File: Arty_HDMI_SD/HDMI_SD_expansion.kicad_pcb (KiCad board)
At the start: 4 copper layers, 109 x 40 mm, 54 parts, among them J2 1140084168, J4 2000-1-2-41-00-BK, J5 UE27AC54100, U1 TPS61232DRCT, U2 MAX3421EEHJ, Y1 KX-7_12,MHz

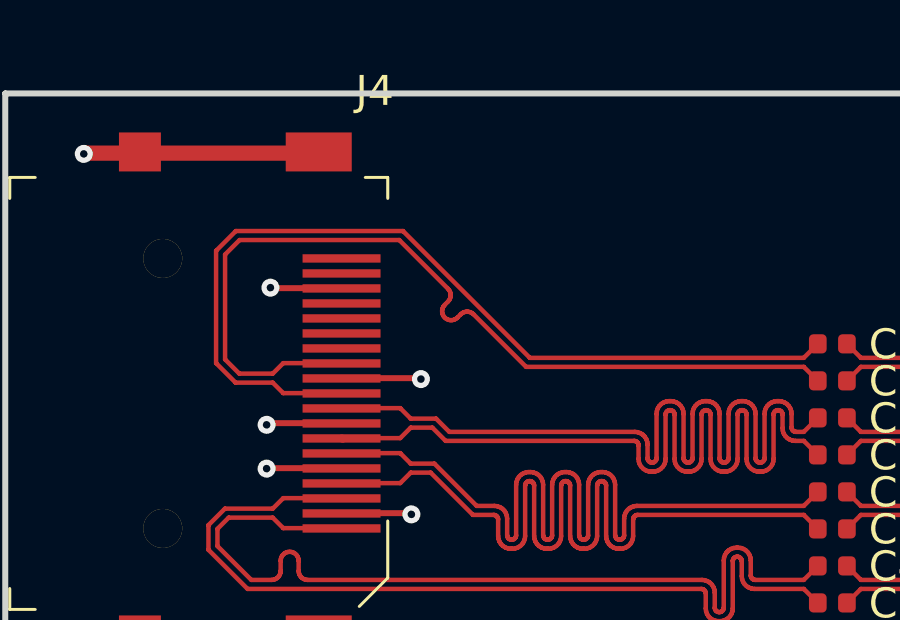
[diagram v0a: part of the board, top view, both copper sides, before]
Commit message: Added more testpads
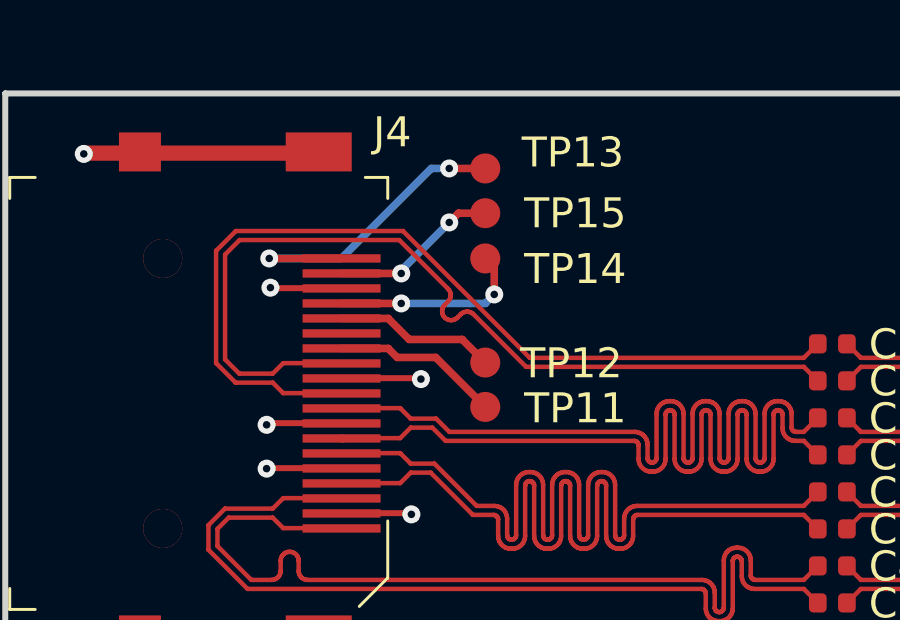
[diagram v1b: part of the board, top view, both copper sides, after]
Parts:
- added TP11: TP_SMD1MM, antmicro-footprints:Testpoint_smd_1mm, F.Cu at (107.7, 95.0)
- added TP12: TP_SMD1MM, antmicro-footprints:Testpoint_smd_1mm, F.Cu at (107.7, 93.5)
- added TP13: TP_SMD1MM, antmicro-footprints:Testpoint_smd_1mm, F.Cu at (107.7, 87.0)
- added TP14: TP_SMD1MM, antmicro-footprints:Testpoint_smd_1mm, F.Cu at (107.7, 90.0)
- added TP15: TP_SMD1MM, antmicro-footprints:Testpoint_smd_1mm, F.Cu at (107.7, 88.5)
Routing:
- net Net-(J4-Pad19): track 0.00 -> 10.9 mm, vias 0 -> 2
- net Net-(J4-Pad16): track 0.00 -> 6.54 mm, vias 0 -> 2
- net Net-(J4-Pad18): track 0.00 -> 5.68 mm, vias 0 -> 2
- net Net-(J4-Pad13): track 0.00 -> 5.60 mm
- net Net-(J4-Pad15): track 0.00 -> 5.40 mm
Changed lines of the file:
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@@
-(kicad_pcb (version 20171130) (host pcbnew 5.0.2+dfsg1-1)
+(kicad_pcb (version 20171130) (host pcbnew 5.0.2+dfsg1-1~bpo9+1)
   (general
     (thickness 1.6)
     (drawings 16)
-    (tracks 2859)
+    (tracks 2889)
     (zones 0)
-    (modules 54)
+    (modules 59)
     (nets 71)
   )
@@
     (1 In1.Cu signal hide)
     (2 In2.Cu signal hide)
-    (31 B.Cu signal hide)
+    (31 B.Cu signal)
     (32 B.Adhes user hide)
     (33 F.Adhes user hide)
@@
     (35 F.Paste user hide)
     (36 B.SilkS user hide)
-    (37 F.SilkS user hide)
+    (37 F.SilkS user)
     (38 B.Mask user hide)
     (39 F.Mask user hide)
@@
   )
   (setup
-    (last_trace_width 0.2)
+    (last_trace_width 0.254)
     (user_trace_width 0.2)
     (user_trace_width 0.508)
@@
     (add_net "Net-(U2-Pad9)")
   )
+  (module antmicro-footprints:Testpoint_smd_1mm (layer F.Cu)
+    (at 107.651241 94.978709)
+    (fp_text reference TP11 (at 3 0) (layer F.SilkS)
+      (effects (font (size 1 1) (thickness 0.15)))
+    )
+    (fp_text value TP_SMD1MM (at 0 -0.5) (layer F.Fab) hide
+      (effects (font (size 1 1) (thickness 0.15)))
+    )
+    (pad 1 smd circle (at 0 -0.0508) (size 1 1) (layers F.Cu F.Paste F.Mask)
+      (net 64 "Net-(J4-Pad13)"))
+  )
+  (module antmicro-footprints:Testpoint_smd_1mm (layer F.Cu)
+    (at 107.651241 93.499509)
+    (fp_text reference TP12 (at 2.87 -0.0208) (layer F.SilkS)
+      (effects (font (size 1 1) (thickness 0.15)))
+    )
+    (fp_text value TP_SMD1MM (at 0 -0.5) (layer F.Fab) hide
+      (effects (font (size 1 1) (thickness 0.15)))
+    )
+    (pad 1 smd circle (at 0 -0.0508) (size 1 1) (layers F.Cu F.Paste F.Mask)
+      (net 66 "Net-(J4-Pad15)"))
+  )
+  (module antmicro-footprints:Testpoint_smd_1mm (layer F.Cu)
+    (at 107.651241 90.029509)
+    (fp_text reference TP14 (at 3 0.3048) (layer F.SilkS)
+      (effects (font (size 1 1) (thickness 0.15)))
+    )
+    (fp_text value TP_SMD1MM (at 0 -0.5) (layer F.Fab) hide
+      (effects (font (size 1 1) (thickness 0.15)))
+    )
+    (pad 1 smd circle (at 0 -0.0508) (size 1 1) (layers F.Cu F.Paste F.Mask)
+      (net 67 "Net-(J4-Pad16)"))
+  )
+  (module antmicro-footprints:Testpoint_smd_1mm (layer F.Cu)
+    (at 107.651241 88.521509)
+    (fp_text reference TP15 (at 3 -0.0428) (layer F.SilkS)
+      (effects (font (size 1 1) (thickness 0.15)))
+    )
+    (fp_text value TP_SMD1MM (at 0 -0.5) (layer F.Fab) hide
+      (effects (font (size 1 1) (thickness 0.15)))
+    )
+    (pad 1 smd circle (at 0 -0.0508) (size 1 1) (layers F.Cu F.Paste F.Mask)
+      (net 68 "Net-(J4-Pad18)"))
+  )
+  (module antmicro-footprints:Testpoint_smd_1mm (layer F.Cu)
+    (at 107.651241 87.029509)
+    (fp_text reference TP13 (at 2.92 -0.58) (layer F.SilkS)
+      (effects (font (size 1 1) (thickness 0.15)))
+    )
+    (fp_text value TP_SMD1MM (at 0 -0.5) (layer F.Fab) hide
+      (effects (font (size 1 1) (thickness 0.15)))
+    )
+    (pad 1 smd circle (at 0 -0.0508) (size 1 1) (layers F.Cu F.Paste F.Mask)
+      (net 69 "Net-(J4-Pad19)"))
+  )
   (module antmicro-footprints:PinHeader_6x2_P2.54mm_Horizontal_Mirrored (layer F.Cu)
     (at 150.651241 117.978709 90)
@@
     (descr http://media.digikey.com/pdf/Data%20Sheets/CNC%20Tech%20PDFs/HDMI_A_Female_2000-1-2-41-00-BK_Dwg.pdf)
     (attr smd)
-    (fp_text reference J4 (at 10.079709 5.565259 180) (layer F.SilkS)
+    (fp_text reference J4 (at 8.7 6.15 180) (layer F.SilkS)
       (effects (font (size 1 1) (thickness 0.15)))
     )
@@
   (segment (start 105.8635 114.15595) (end 105.62695 114.3925) (width 0.15) (layer F.Cu) (net 63))
   (segment (start 105.62695 114.3925) (end 105.0015 114.3925) (width 0.15) (layer F.Cu) (net 63))
+  (segment (start 104.415241 92.978709) (end 104.715241 93.278709) (width 0.254) (layer F.Cu) (net 64))
+  (segment (start 102.861241 92.978709) (end 104.415241 92.978709) (width 0.254) (layer F.Cu) (net 64))
+  (segment (start 106.002041 93.278709) (end 107.651241 94.927909) (width 0.254) (layer F.Cu) (net 64))
+  (segment (start 104.715241 93.278709) (end 106.002041 93.278709) (width 0.254) (layer F.Cu) (net 64))
+  (segment (start 104.415241 91.978709) (end 105.115241 92.678709) (width 0.254) (layer F.Cu) (net 66))
+  (segment (start 102.861241 91.978709) (end 104.415241 91.978709) (width 0.254) (layer F.Cu) (net 66))
+  (segment (start 106.881241 92.678709) (end 107.651241 93.448709) (width 0.254) (layer F.Cu) (net 66))
+  (segment (start 105.115241 92.678709) (end 106.881241 92.678709) (width 0.254) (layer F.Cu) (net 66))
+  (via (at 104.851241 91.478709) (size 0.6) (drill 0.25) (layers F.Cu B.Cu) (net 67))
+  (segment (start 102.861241 91.478709) (end 104.851241 91.478709) (width 0.254) (layer F.Cu) (net 67))
+  (segment (start 104.851241 91.478709) (end 107.151241 91.478709) (width 0.254) (layer B.Cu) (net 67))
+  (segment (start 107.151241 91.478709) (end 107.651241 91.478709) (width 0.254) (layer B.Cu) (net 67))
+  (via (at 107.951241 91.178709) (size 0.6) (drill 0.25) (layers F.Cu B.Cu) (net 67))
+  (segment (start 107.651241 91.478709) (end 107.951241 91.178709) (width 0.254) (layer B.Cu) (net 67))
+  (segment (start 107.951241 90.278709) (end 107.651241 89.978709) (width 0.254) (layer F.Cu) (net 67))
+  (segment (start 107.951241 91.178709) (end 107.951241 90.278709) (width 0.254) (layer F.Cu) (net 67))
+  (via (at 104.851241 90.478709) (size 0.6) (drill 0.25) (layers F.Cu B.Cu) (net 68))
+  (segment (start 102.861241 90.478709) (end 104.851241 90.478709) (width 0.254) (layer F.Cu) (net 68))
+  (via (at 106.451241 88.778709) (size 0.6) (drill 0.25) (layers F.Cu B.Cu) (net 68))
+  (segment (start 104.851241 90.378709) (end 106.451241 88.778709) (width 0.254) (layer B.Cu) (net 68))
+  (segment (start 104.851241 90.478709) (end 104.851241 90.378709) (width 0.254) (layer B.Cu) (net 68))
+  (segment (start 106.759241 88.470709) (end 106.451241 88.778709) (width 0.254) (layer F.Cu) (net 68))
+  (segment (start 107.651241 88.470709) (end 106.759241 88.470709) (width 0.254) (layer F.Cu) (net 68))
+  (via (at 100.451241 89.978709) (size 0.6) (drill 0.25) (layers F.Cu B.Cu) (net 69))
+  (segment (start 102.861241 89.978709) (end 100.451241 89.978709) (width 0.254) (layer F.Cu) (net 69))
+  (segment (start 100.451241 89.978709) (end 102.851241 89.978709) (width 0.254) (layer B.Cu) (net 69))
+  (segment (start 102.851241 89.978709) (end 105.851241 86.978709) (width 0.254) (layer B.Cu) (net 69))
+  (via (at 106.451241 86.978709) (size 0.6) (drill 0.25) (layers F.Cu B.Cu) (net 69))
+  (segment (start 105.851241 86.978709) (end 106.451241 86.978709) (width 0.254) (layer B.Cu) (net 69))
+  (segment (start 106.451241 86.978709) (end 107.651241 86.978709) (width 0.254) (layer F.Cu) (net 69))
   (zone (net 2) (net_name GND) (layer In1.Cu) (hatch edge 0.508)
     (connect_pads (clearance 0.508))
